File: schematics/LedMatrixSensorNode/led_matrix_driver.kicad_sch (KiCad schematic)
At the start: 30 parts, among them J1 LED Matrrix, SW1 Button 1, SW2 Button 2, U1 SM5166PF, U2 SM5166PF, U3 SM5166PF, U4 DS1302Z+, U5 SM16306SJ, U6 SM16306SJ, U7 SM16306SJ, Y1 32768KHz

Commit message: Added WI-Fi config, OTA, CO2, temperature, humidity sensors, MQTT for sensors
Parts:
- renumbered C3 to C1, C9 to C10, C12 to C11, C13 to C12, C14 to C13, C8 to C2, C4 to C3, C7 to C4, C1 to C7, C2 to C8, C11 to C8, C10 to C9, R2 to R1, R3 to R2, R4 to R3, R1 to R4, SW2 to SW?, SW1 to SW?, U5 to U4, U6 to U5, U7 to U6, U4 to U7

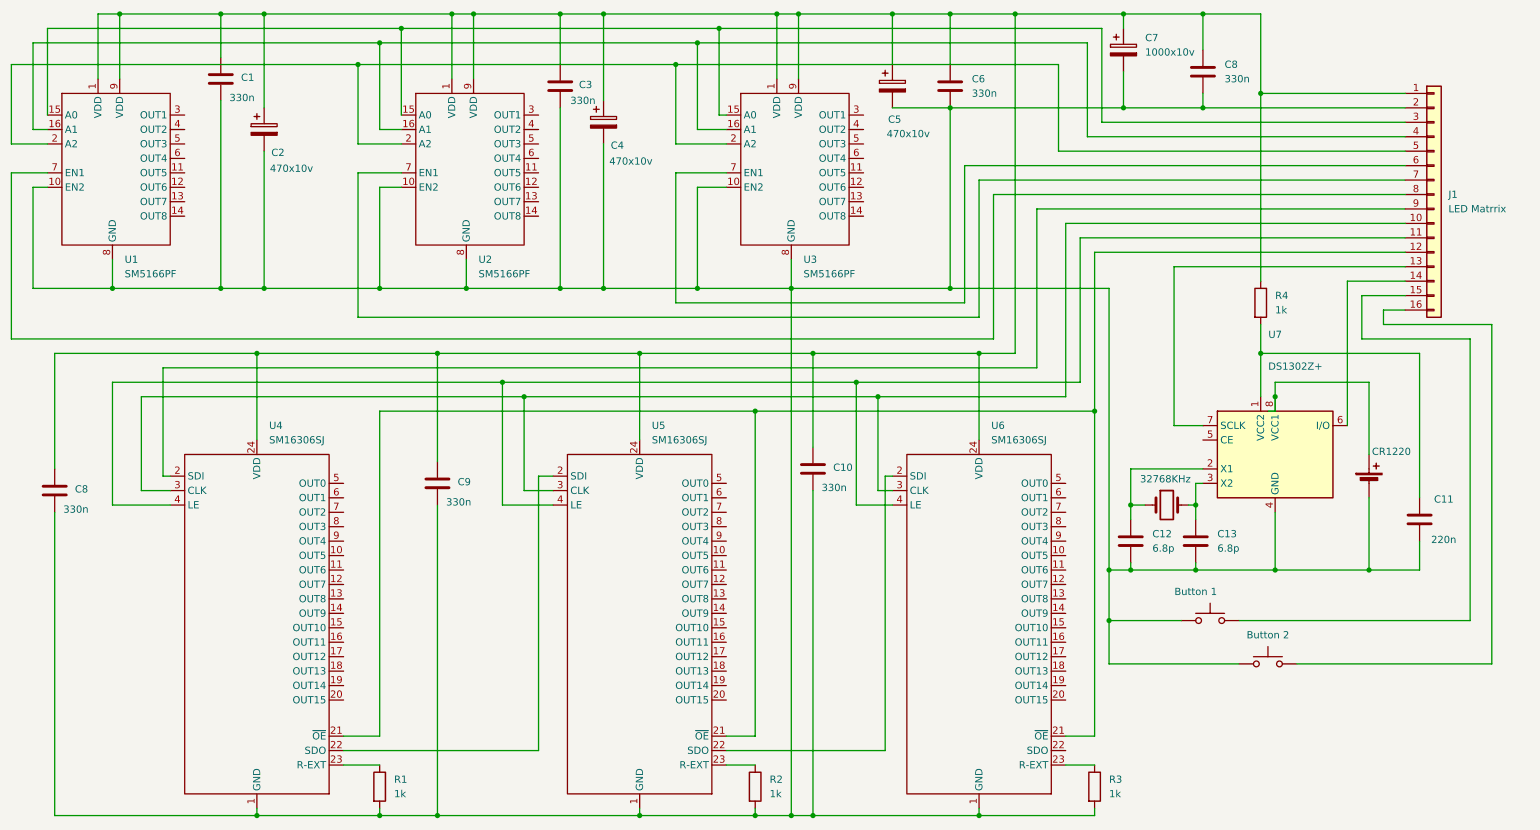
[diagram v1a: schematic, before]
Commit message: Added MQTT mode, message, beeper, LED clock, temp, CO2, message, auto LED brightness, mode / LED off buttons
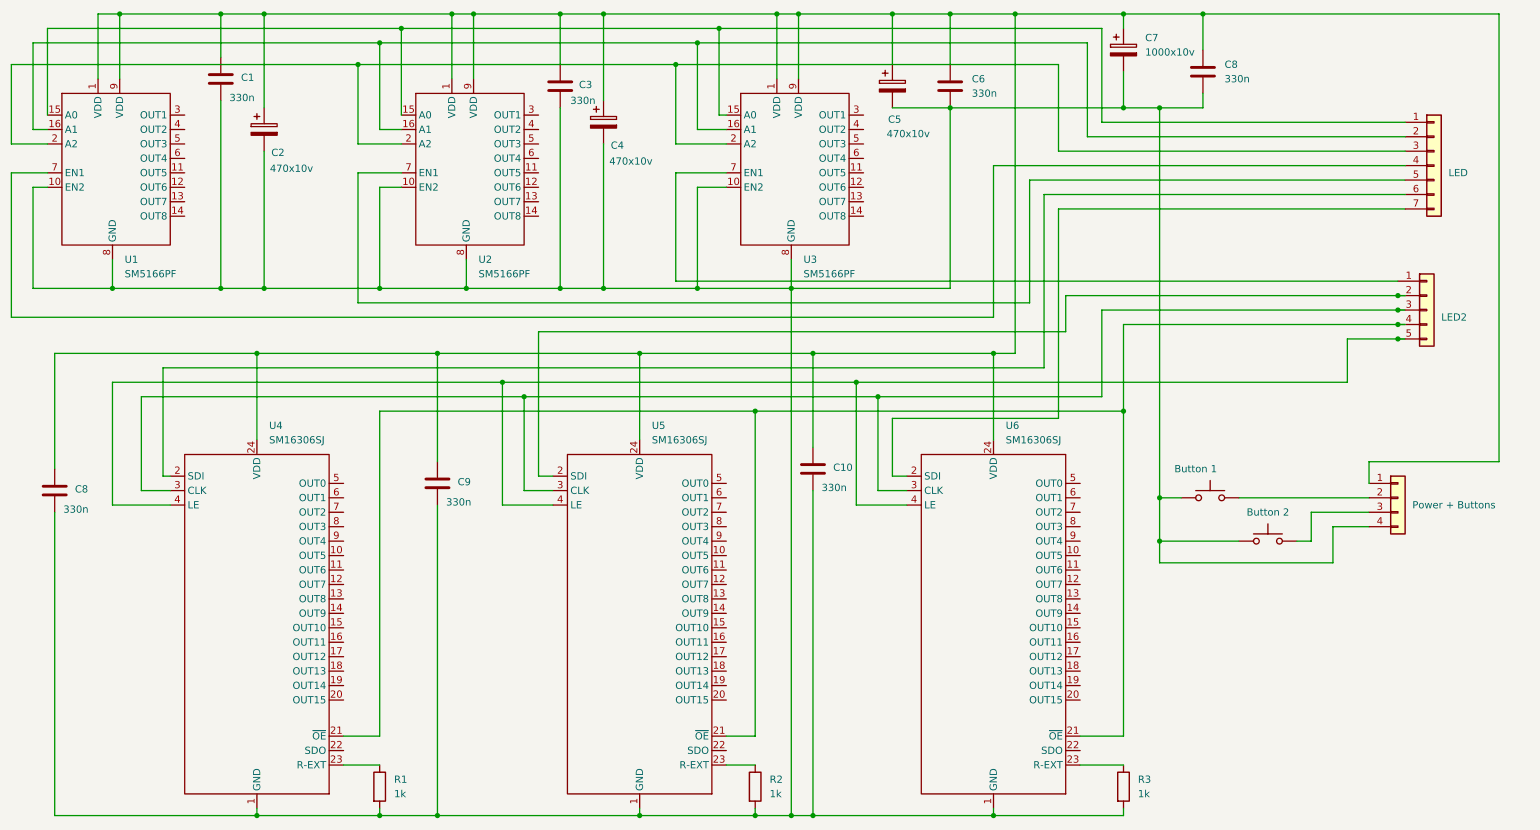
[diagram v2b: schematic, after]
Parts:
- removed BT1: CR1220, symbol Device:Battery_Cell
- removed C11: 220n, symbol Device:C
- removed C12, C13: 6.8p, symbol Device:C
- removed J1: LED Matrrix, symbol Connector_Generic:Conn_01x16
- removed R4: 1k, symbol Device:R
- removed U7: DS1302Z+, Package_SO:SOIC-8_3.9x4.9mm_P1.27mm, symbol Timer_RTC:DS1302Z+
- removed Y1: 32768KHz, symbol Device:Crystal
- added J10: LED2, symbol Connector_Generic:Conn_01x05
- added J11: Power + Buttons, symbol Connector_Generic:Conn_01x04
- added J13: LED, symbol Connector_Generic:Conn_01x07
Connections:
- net at C1.1, C10.1, C2.1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: now also J11.1 (Pin_1)
- net at C1.2, C10.2, C2.2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: now also J11.4 (Pin_4)
- net at U5.2 (SDI): now also J10.2 (Pin_2); no longer U4.22 (SDO)
- net at U4.21 (~{OE}), U5.21 (~{OE}), U6.21 (~{OE}): now also J10.4 (Pin_4)
- net at U5.22 (SDO): no longer U6.2 (SDI)
- net at U4.3 (CLK), U5.3 (CLK), U6.3 (CLK): now also J10.3 (Pin_3)
- net at U4.4 (LE), U5.4 (LE), U6.4 (LE): now also J10.5 (Pin_5)
- net at SW?.2: now also J11.3 (Pin_3)
- net at SW?.2: now also J11.2 (Pin_2)
- net at U1.15 (A0), U2.15 (A0), U3.15 (A0): now also J13.1 (Pin_1)
- net at U1.16 (A1), U2.16 (A1), U3.16 (A1): now also J13.2 (Pin_2)
- net at U1.2 (A2), U2.2 (A2), U3.2 (A2): now also J13.3 (Pin_3)
- net at U2.7 (EN1): now also J13.5 (Pin_5)
- net at U3.7 (EN1): now also J10.1 (Pin_1)
- net at U4.2 (SDI): now also J13.6 (Pin_6)
- net at U1.7 (EN1): now also J13.4 (Pin_4)
- new net: J13.7 (Pin_7), U6.2 (SDI)
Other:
- moved on the sheet: R3, U6
